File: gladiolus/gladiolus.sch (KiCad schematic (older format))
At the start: 133 parts, among them J1 NEIGHBOR1, J2 NEIGHBOR2, J7 BONUS_ROW, P1 CONN_01X05, Q1 Q_NPN_BEC, U1 THS4520RGT, U2 AD8330ARQZ, U3 AD9283, U4 AD9704, U5 LMH6643

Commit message: Added AC/DC coupling switch and removed central header
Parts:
- removed P1: CONN_01X05, gsg-modules:HEADER-1x5, symbol CONN_01X05
- added C28: 8nF, gsg-modules:0603, symbol Device:C
- added Q2: BS, Package_TO_SOT_THT:TO-92_Inline, symbol Transistor_FET:BS107
- added R76: 1M, gsg-modules:0603, symbol Device:R
- C1, C10, C11, C12, C13, C14, C15, C16, C17, C18, C19, C2, C20, C21, C22, C23, C24, C25, C26, C27, C3, C4, C5, C6, C7, C8, C9: symbol C -> Device:C
- D1, D2: symbol D -> Device:D
- D3: symbol LED -> gladiolus-rescue:LED
- FB1: symbol FILTER -> gladiolus-rescue:FILTER
- J1, J2: symbol CONN_02X20 -> gladiolus-rescue:CONN_02X20
- J7: symbol CONN_01X20 -> gladiolus-rescue:CONN_01X20
- L1, L10, L2, L3, L4, L5, L6, L7, L8, L9: symbol L_Small -> Device:L_Small
- MH1, MH2, MH3, MH4: symbol CONN_01X01 -> gladiolus-rescue:CONN_01X01
- Q1: symbol Q_NPN_BEC -> Device:Q_NPN_BEC
- R1, R10, R11, R12, R13, R14, R15, R16, R17, R18, R19, R2, R20, R21, R22, R23, R24, R25, R26, R27, R28, R29, R3, R30, R31, R32, R33, R34, R35, R36, R37, R38, R39, R4, R40, R41, R42, R43, R44, R45, R46, R47, R48, R49, R5, R50, R51, R52, R53, R54, R55, R56, R57, R58, R59, R6, R60, R61, R62, R63, R64, R65, R66, R67, R68, R69, R7, R70, R71, R72, R73, R74, R75, R8, R9: symbol R -> Device:R
- RV1, RV2, RV3: symbol POT -> gladiolus-rescue:POT
- U1: symbol THS4520RGT -> gladiolus-rescue:THS4520RGT
- U2: symbol AD8330ARQZ -> gladiolus-rescue:AD8330ARQZ
- U3: symbol AD9283 -> gladiolus-rescue:AD9283
- U4: symbol AD9704 -> gladiolus-rescue:AD9704
- U5: symbol LMH6643 -> gladiolus-rescue:LMH6643
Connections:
- wire segments 492 -> 588
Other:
- note added: "switch for\nac/dc coupling"
- note removed: "P1 blocks direct light from TX to RX"

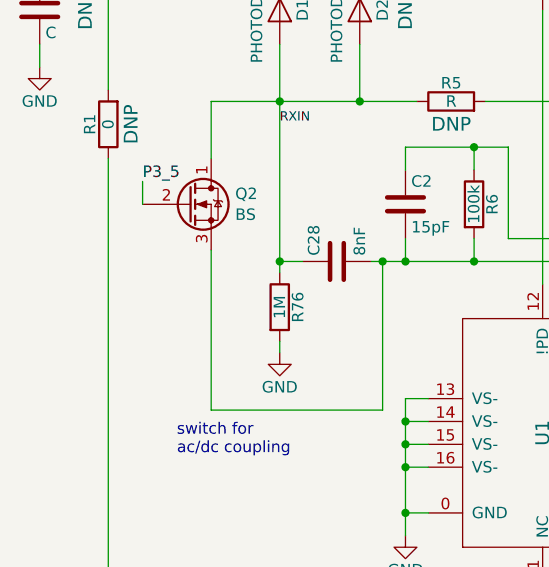
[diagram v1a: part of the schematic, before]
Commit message: Added transistor notes
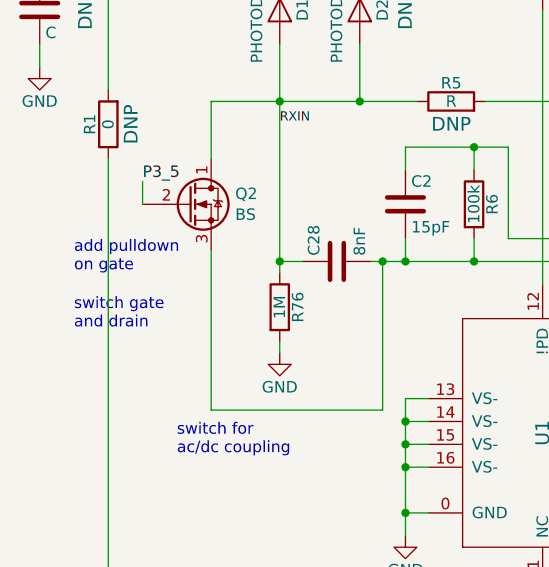
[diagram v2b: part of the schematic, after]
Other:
- note added: "add pulldown\non gate"
- note added: "switch gate \nand drain"
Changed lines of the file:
@@
 Text Notes 1200 3500 0    50   ~ 0
 switch for\nac/dc coupling
+Text Notes 750  2700 0    50   ~ 0
+add pulldown\non gate
+Text Notes 750  2950 0    50   ~ 0
+switch gate \nand drain
 $EndSCHEMATC

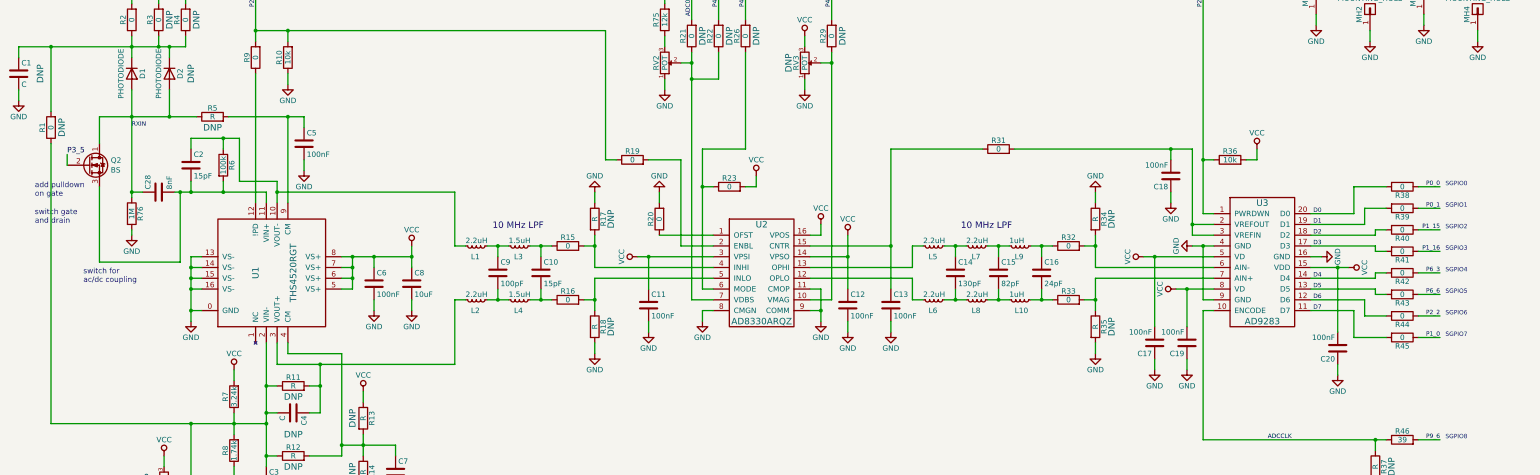
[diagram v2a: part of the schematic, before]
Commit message: Added AC/DC coupling switch using 74LVC1G3157
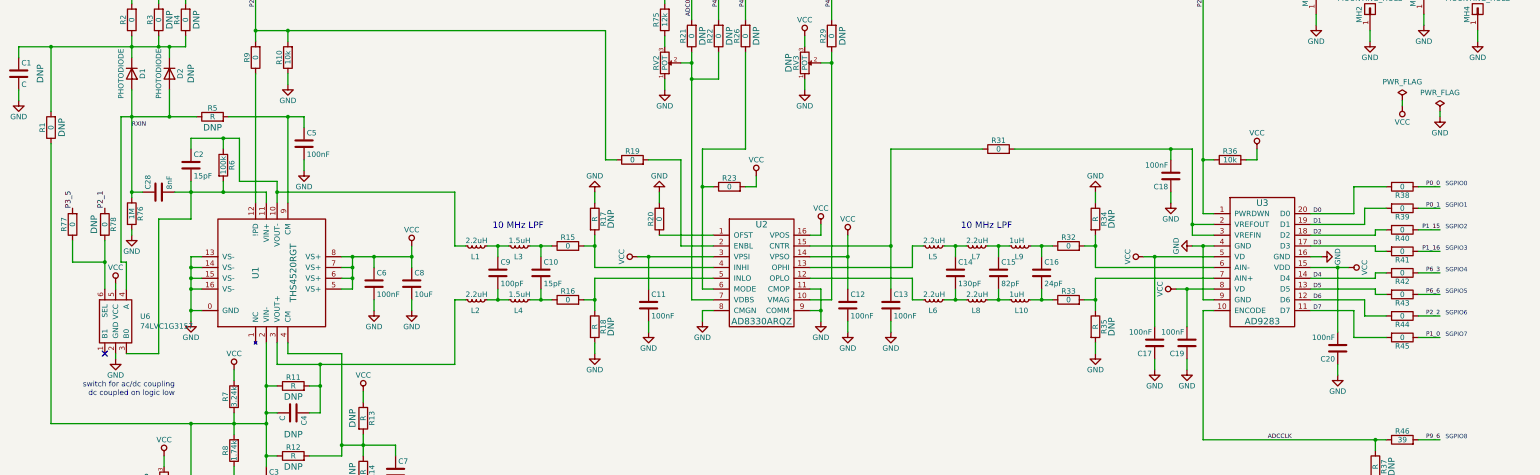
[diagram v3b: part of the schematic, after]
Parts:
- removed Q2: BS, Package_TO_SOT_THT:TO-92_Inline, symbol Transistor_FET:BS107
- added R77, R78: 0, gsg-modules:0603, symbol Device:R
- added U6: 74LVC1G3157, gsg-modules:SOT363, symbol gsg-symbols:74LVC1G3157
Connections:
- net GND: now also U6.2 (GND)
- net P2_1: now also R78.1
- net P3_5: now also R77.2
- net RXIN: now also U6.4 (A)
- net VCC: now also U6.5 (VCC)
- net at C2.2, C28.2, R6.2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: now also U6.3 (B0)
- new net: R77.1, R78.2, U6.6 (SEL)
- no-connect marks 2 -> 3
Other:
- note added: "switch for ac/dc coupling\ndc coupled on logic low"
- note removed: "add pulldown\non gate"
- note removed: "switch for\nac/dc coupling"
- note removed: "switch gate \nand drain"
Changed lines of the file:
@@
 Connection ~ 1650 1950
-$Comp
-L Transistor_FET:BS107 Q2
-U 1 1 5C70F3A6
-P 1250 2400
-F 0 "Q2" H 1455 2446 50  0000 L CNN
-F 1 "BS" H 1455 2355 50  0000 L CNN
-F 2 "Package_TO_SOT_THT:TO-92_Inline" H 1450 2325 50  0001 L CIN
-F 3 "http://www.onsemi.com/pub_link/Collateral/BS107-D.PDF" H 1250 2400 50  0001 L CNN
-	1    1250 2400
-	1    0    0    -1
-$EndComp
 $Comp
 L Device:C C28
@@
 Wire Wire Line
 	1650 2650 1650 2700
+Connection ~ 2200 2650
+Text Notes 2050 4550 2    50   ~ 0
+switch for ac/dc coupling\ndc coupled on logic low
+$Comp
+L power:PWR_FLAG #FLG0101
+U 1 1 5C7387E5
+P 13450 1800
+F 0 "#FLG0101" H 13450 1875 50  0001 C CNN
+F 1 "PWR_FLAG" H 13450 1974 50  0000 C CNN
+F 2 "" H 13450 1800 50  0001 C CNN
+F 3 "~" H 13450 1800 50  0001 C CNN
+	1    13450 1800
+	1    0    0    -1
+$EndComp
+$Comp
+L power:PWR_FLAG #FLG0102
+U 1 1 5C739087
+P 13800 1900
+F 0 "#FLG0102" H 13800 1975 50  0001 C CNN
+F 1 "PWR_FLAG" H 13800 2074 50  0000 C CNN
+F 2 "" H 13800 1900 50  0001 C CNN
+F 3 "~" H 13800 1900 50  0001 C CNN
+	1    13800 1900
+	1    0    0    -1
+$EndComp
+$Comp
+L power:VCC #PWR0102
+U 1 1 5C7394DA
+P 13450 1850
+F 0 "#PWR0102" H 13450 1700 50  0001 C CNN
+F 1 "VCC" H 13450 2000 50  0000 C CNN
+F 2 "" H 13450 1850 60  0000 C CNN
+F 3 "" H 13450 1850 60  0000 C CNN
+	1    13450 1850
+	-1   0    0    1
+$EndComp
+$Comp
+L power:GND #PWR0103
+U 1 1 5C739A3F
+P 13800 1950
+F 0 "#PWR0103" H 13800 1700 50  0001 C CNN
+F 1 "GND" H 13800 1800 50  0000 C CNN
+F 2 "" H 13800 1950 50  0000 C CNN
+F 3 "" H 13800 1950 50  0000 C CNN
+	1    13800 1950
+	1    0    0    -1
+$EndComp
 Wire Wire Line
-	2050 2650 2100 2650
-Connection ~ 2200 2650
+	13450 1800 13450 1850
 Wire Wire Line
-	1350 2200 1350 1950
+	13800 1900 13800 1950
+$Comp
+L gsg-symbols:74LVC1G3157 U6
+U 1 1 5C5F46ED
+P 1500 3850
+F 0 "U6" V 1546 3622 50  0000 R CNN
+F 1 "74LVC1G3157" V 1455 3622 50  0000 R CNN
+F 2 "gsg-modules:SOT363" H 1500 3850 50  0001 C CNN
+F 3 "" H 1500 3850 50  0001 C CNN
+F 4 "Diodes Incorporated" V 1455 3622 50  0001 R CNN "Manufacturer"
+F 5 "74LVC1G3157DW-7" H 1500 3850 50  0001 C CNN "Part Number"
+F 6 "IC SWITCH SPDT 6 OHM SOT363" V 1364 3622 50  0001 R CNN "Description"
+	1    1500 3850
+	0    -1   -1   0
+$EndComp
+Text Label 1100 2800 1    50   ~ 0
+P3_5
 Wire Wire Line
-	1350 1950 1650 1950
+	1500 4150 1500 4200
 Wire Wire Line
-	1350 2600 1350 3300
+	1500 3550 1500 3500
+$Comp
+L power:GND #PWR0104
+U 1 1 5C70B620
+P 1500 4200
+F 0 "#PWR0104" H 1500 3950 50  0001 C CNN
+F 1 "GND" H 1500 4050 50  0000 C CNN
+F 2 "" H 1500 4200 50  0000 C CNN
+F 3 "" H 1500 4200 50  0000 C CNN
+	1    1500 4200
+	1    0    0    -1
+$EndComp
+$Comp
+L power:VCC #PWR0105
+U 1 1 5C70CA81
+P 1500 3500
+F 0 "#PWR0105" H 1500 3350 50  0001 C CNN
+F 1 "VCC" H 1500 3650 50  0000 C CNN
+F 2 "" H 1500 3500 60  0000 C CNN
+F 3 "" H 1500 3500 60  0000 C CNN
+	1    1500 3500
+	1    0    0    -1
+$EndComp
 Wire Wire Line
-	1350 3300 2100 3300
+	2050 2650 2200 2650
 Wire Wire Line
-	2100 3300 2100 2650
-Connection ~ 2100 2650
+	1650 1950 1550 1950
 Wire Wire Line
-	2100 2650 2200 2650
+	1550 1950 1550 3300
 Wire Wire Line
-	1050 2400 1050 2300
-Text Label 1050 2300 0    50   ~ 0
-P3_5
-Text Notes 1200 3500 0    50   ~ 0
-switch for\nac/dc coupling
-Text Notes 750  2700 0    50   ~ 0
-add pulldown\non gate
-Text Notes 750  2950 0    50   ~ 0
-switch gate \nand drain
+	1550 3300 1600 3300
+Wire Wire Line
+	1600 3300 1600 3550
+Wire Wire Line
+	1600 4150 1900 4150
+Wire Wire Line
+	1900 4150 1900 2900
+Wire Wire Line
+	1900 2900 2200 2900
+Wire Wire Line
+	2200 2900 2200 2650
+NoConn ~ 1400 4150
+$Comp
+L Device:R R77
+U 1 1 5C8E0748
+P 1100 2950
+F 0 "R77" V 1180 2950 50  0000 C CNN
+F 1 "0" V 1100 2950 50  0000 C CNN
+F 2 "gsg-modules:0603" V 1030 2950 50  0001 C CNN
+F 3 "" H 1100 2950 50  0000 C CNN
+F 4 "Yageo" H 1100 2950 60  0001 C CNN "Manufacturer"
+F 5 "RC0603JR-070RL" H 1100 2950 60  0001 C CNN "Part Number"
+F 6 "RES SMD 0.0OHM JUMPER 1/10W 0603" H 1100 2950 60  0001 C CNN "Description"
+	1    1100 2950
+	-1   0    0    1
+$EndComp
+$Comp
+L Device:R R78
+U 1 1 5C8E1B74
+P 1400 2950
+F 0 "R78" V 1480 2950 50  0000 C CNN
+F 1 "0" V 1400 2950 50  0000 C CNN
+F 2 "gsg-modules:0603" V 1330 2950 50  0001 C CNN
+F 3 "" H 1400 2950 50  0000 C CNN
+F 4 "DNP" V 1300 2950 60  0000 C CNN "Note"
+	1    1400 2950
+	1    0    0    -1
+$EndComp
+Wire Wire Line
+	1100 3100 1100 3300
+Wire Wire Line
+	1100 3300 1400 3300
+Wire Wire Line
+	1400 3300 1400 3550
+Wire Wire Line
+	1400 3100 1400 3300
+Connection ~ 1400 3300
+Text Label 1400 2800 1    50   ~ 0
+P2_1
 $EndSCHEMATC

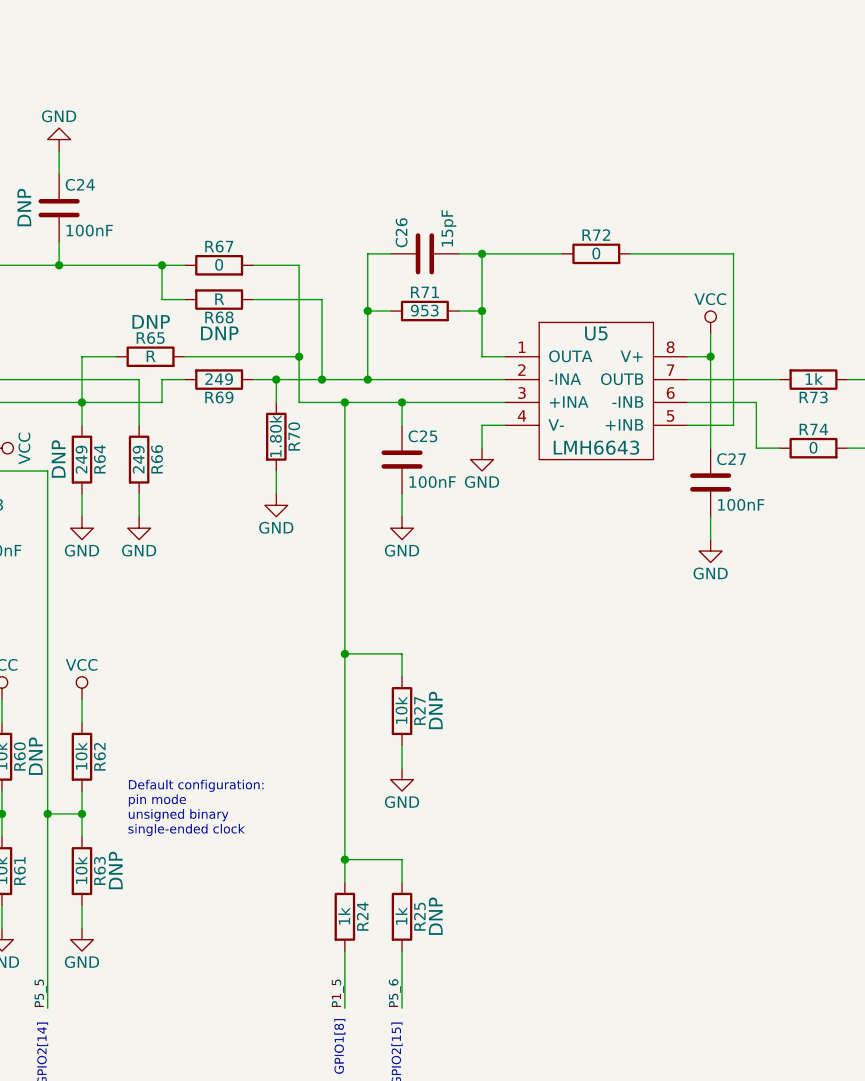
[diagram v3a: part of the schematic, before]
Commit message: Added TODO design notes
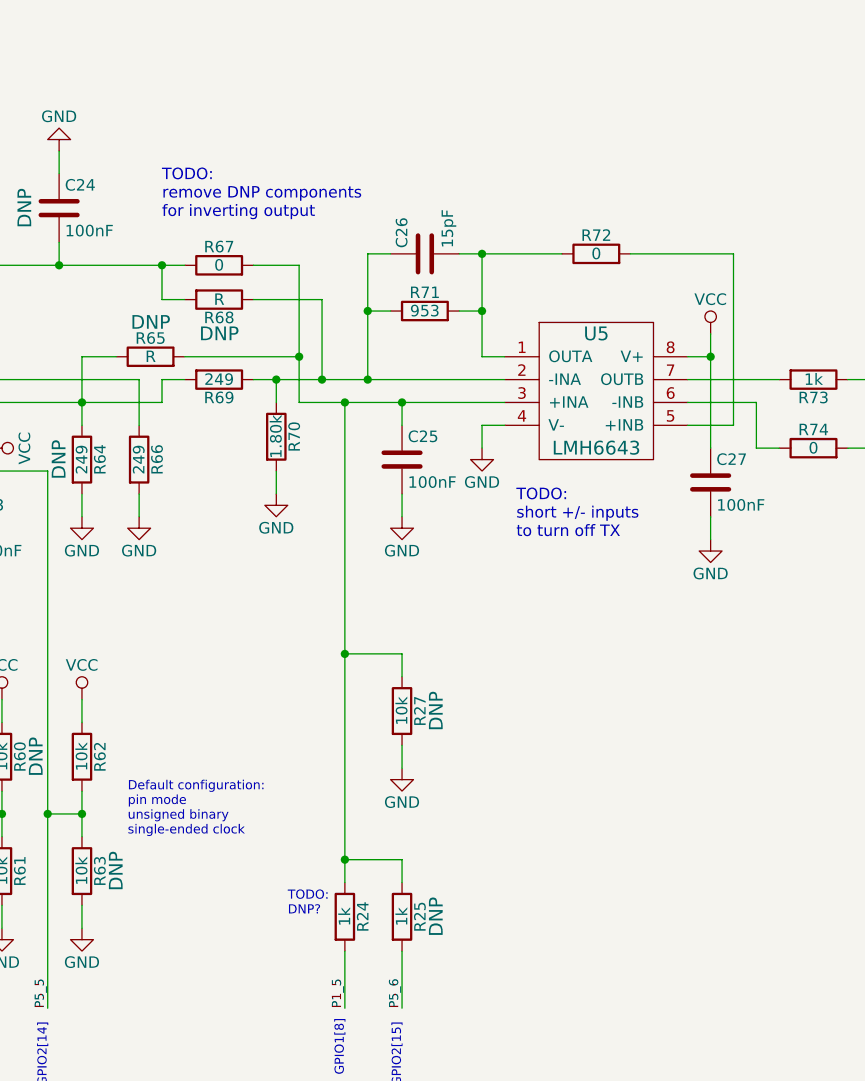
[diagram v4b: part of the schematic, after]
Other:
- note added: "TODO:\nDNP?"
- note added: "TODO:\nremove DNP components\nfor inverting output"
- note added: "TODO:\nshort +/- inputs\nto turn off TX"
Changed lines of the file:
@@
 Text Label 1400 2800 1    50   ~ 0
 P2_1
+Text Notes 5600 9750 0    40   ~ 0
+TODO:\nDNP?
+Text Notes 6600 8100 0    50   ~ 0
+TODO:\nshort +/- inputs\nto turn off TX
+Text Notes 5050 6700 0    50   ~ 0
+TODO:\nremove DNP components\nfor inverting output
 $EndSCHEMATC

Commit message: Gladiolus: Added AD/DC coupling switch, removed DNP components for inversion, added switch to fully turn off TX, routed TX LED current to ADC
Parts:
- removed R68: R, gsg-modules:0603, symbol Device:R
- added C29: 470pF, gsg-modules:0402, symbol Device:C
- added U7: 74LVC1G3157, gsg-modules:SOT363, symbol gsg-symbols:74LVC1G3157
- D3: symbol gladiolus-rescue:LED -> gladiolus-rescue:LED-gladiolus-rescue
- FB1: symbol gladiolus-rescue:FILTER -> gladiolus-rescue:FILTER-gladiolus-rescue
- J1, J2: symbol gladiolus-rescue:CONN_02X20 -> gladiolus-rescue:CONN_02X20-gladiolus-rescue
- J7: symbol gladiolus-rescue:CONN_01X20 -> gladiolus-rescue:CONN_01X20-gladiolus-rescue
- MH1, MH2, MH3, MH4: symbol gladiolus-rescue:CONN_01X01 -> gladiolus-rescue:CONN_01X01-gladiolus-rescue
- R64: value 249 -> 0; Description RES SMD 249 OHM 1% 1/10W 0603 -> RES SMD 0.0OHM JUMPER 1/10W 0603; Part Number 311-249HR -> RC0603JR-070RL
- R65: value R -> 0; Description (none) -> RES SMD 0.0OHM JUMPER 1/10W 0603; Manufacturer (none) -> Yageo; Part Number (none) -> RC0603JR-070RL
- RV1, RV2, RV3: symbol gladiolus-rescue:POT -> gladiolus-rescue:POT-gladiolus-rescue
- U1: symbol gladiolus-rescue:THS4520RGT -> gladiolus-rescue:THS4520RGT-gladiolus-rescue
- U2: symbol gladiolus-rescue:AD8330ARQZ -> gladiolus-rescue:AD8330ARQZ-gladiolus-rescue
- U3: symbol gladiolus-rescue:AD9283 -> gladiolus-rescue:AD9283-gladiolus-rescue
- U4: symbol gladiolus-rescue:AD9704 -> gladiolus-rescue:AD9704-gladiolus-rescue
- U5: symbol gladiolus-rescue:LMH6643 -> gladiolus-rescue:LMH6643-gladiolus-rescue
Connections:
- wire segments 597 -> 605
- no-connect marks 3 -> 63
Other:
- note added: "^ This cap cuts off\nhigher freqs (15MHz+)\n470pF works well"
- note added: "removed DNP components\nfor inverting output"
- note added: "short +/- inputs\nto turn off TX"
- note added: "switch for ac/dc coupling\nac coupled on logic low"
- note removed: "TODO:\nremove DNP components\nfor inverting output"
- note removed: "TODO:\nshort +/- inputs\nto turn off TX"
- note removed: "switch for ac/dc coupling\ndc coupled on logic low"
- moved on the sheet: Q1, R30, R66, R73, R74

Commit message: Minor change to Gladiolus silkscreen. Began designing Foxglove level shifters / comparators and power supplies.
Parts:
- removed R65: 0, gsg-modules:0603, symbol Device:R
- added J3: Conn_01x02_Female, gsg-modules:HEADER-1x2, symbol Connector:Conn_01x02_Female
- C29: Description (none) -> CAP CER 470PF 50V X7R 0402; Manufacturer (none) -> Murata Electronics North America; Part Number (none) -> GCM155R71H471KA37D
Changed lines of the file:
@@
 F 2 "gsg-modules:0402" H 8038 7550 50  0001 C CNN
 F 3 "" H 8000 7700 50  0000 C CNN
+F 4 "Murata Electronics North America" H 8000 7700 50  0001 C CNN "Manufacturer"
+F 5 "GCM155R71H471KA37D " H 8000 7700 50  0001 C CNN "Part Number"
+F 6 "CAP CER 470PF 50V X7R 0402" H 8000 7700 50  0001 C CNN "Description"
 	1    8000 7700
 	1    0    0    -1
@@
 Wire Wire Line
 	9900 8000 9650 8000
-Wire Wire Line
-	8850 8000 9250 8000
-Text Label 9900 8250 2    40   ~ 0
-P1_17
-$Comp
-L Device:R R65
-U 1 1 5D05915F
-P 9500 8250
-F 0 "R65" V 9580 8250 50  0000 C CNN
-F 1 "0" V 9500 8250 50  0000 C CNN
-F 2 "gsg-modules:0603" V 9430 8250 50  0001 C CNN
-F 3 "" H 9500 8250 50  0000 C CNN
-F 4 "Yageo" H 9500 8250 60  0001 C CNN "Manufacturer"
-F 5 "RC0603JR-070RL" H 9500 8250 60  0001 C CNN "Part Number"
-F 6 "RES SMD 0.0OHM JUMPER 1/10W 0603" H 9500 8250 60  0001 C CNN "Description"
-F 7 "DNP" V 9400 8250 60  0000 C CNN "Note"
-	1    9500 8250
-	0    -1   -1   0
-$EndComp
-Wire Wire Line
-	9900 8250 9650 8250
-Wire Wire Line
-	9250 8000 9250 8250
-Wire Wire Line
-	9250 8250 9350 8250
-Connection ~ 9250 8000
-Wire Wire Line
-	9250 8000 9350 8000
 Wire Wire Line
 	5650 6900 5650 7500
@@
 NoConn ~ 15850 7050
 NoConn ~ 15950 7050
+Wire Wire Line
+	8850 8000 9250 8000
+$Comp
+L Connector:Conn_01x02_Female J3
+U 1 1 5C85EBB0
+P 9600 8200
+F 0 "J3" H 9627 8176 50  0000 L CNN
+F 1 "Conn_01x02_Female" H 9627 8085 50  0000 L CNN
+F 2 "gsg-modules:HEADER-1x2" H 9600 8200 50  0001 C CNN
+F 3 "~" H 9600 8200 50  0001 C CNN
+	1    9600 8200
+	1    0    0    -1
+$EndComp
+Wire Wire Line
+	9250 8000 9250 8200
+Wire Wire Line
+	9250 8200 9400 8200
+Connection ~ 9250 8000
+Wire Wire Line
+	9250 8000 9350 8000
+$Comp
+L power:GND #PWR0108
+U 1 1 5C8BF1A4
+P 9350 8300
+F 0 "#PWR0108" H 9350 8050 50  0001 C CNN
+F 1 "GND" H 9350 8150 50  0000 C CNN
+F 2 "" H 9350 8300 50  0000 C CNN
+F 3 "" H 9350 8300 50  0000 C CNN
+	1    9350 8300
+	0    1    1    0
+$EndComp
+Wire Wire Line
+	9350 8300 9400 8300
 $EndSCHEMATC

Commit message: Lucky Bamboo: Rerouted RX RF signals and rearranged schematic to be consistent with layout. Gladiolus: Routed incomplete signal near TX transistor.
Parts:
- J3: Note (none) -> DNP
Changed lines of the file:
@@
 F 2 "gsg-modules:HEADER-1x2" H 9600 8200 50  0001 C CNN
 F 3 "~" H 9600 8200 50  0001 C CNN
+F 4 "DNP" H 9600 8200 50  0001 C CNN "Note"
 	1    9600 8200
 	1    0    0    -1
